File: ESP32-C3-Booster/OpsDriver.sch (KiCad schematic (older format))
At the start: 14 parts, among them U501 DRV8873HPWPR

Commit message: Completed first pass ESP32-C3-Booster.
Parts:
- added R505: 2.7K, Resistors_SMD:R_0603, symbol R
- added R506, R507: 10K, Resistors_SMD:R_0603, symbol R
- added U502: VO615A, Housings_SOIC:SO-4_7.6x3.6mm_Pitch2.54mm, symbol VO615A
- R501: value 220K -> 10K; Mouser Part Number 279-CRGCQ0603F220K -> 279-CRGCQ0603F10K
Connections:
- net +3V3: now also R506.1, R507.1
- net GND: now also U502.3
- net IN_A: now also R505.2; no longer U501.7 (EN/IN1)
- net IN_B: now also U502.1; no longer U501.8 (PH/IN2)
- new net: R507.2, U501.7 (EN/IN1)
- new net: R506.2, U501.8 (PH/IN2), U502.4
- new net: R505.1, U502.2
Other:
- moved on the sheet: TP501, TP502
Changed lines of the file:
@@
 LIBS:mcp9701at
 LIBS:MCP9700T-E_LT
+LIBS:ina180b
 LIBS:ESP32-C3-Booster-cache
 EELAYER 25 0
@@
 Comment4 ""
 $EndDescr
-Text HLabel 2500 2500 0    60   Input ~ 0
+Text HLabel 1050 2500 0    60   Input ~ 0
 IN_B
-Text HLabel 2500 2400 0    60   Input ~ 0
+Text HLabel 1050 2350 0    60   Input ~ 0
 IN_A
 Text HLabel 2500 2600 0    60   Input ~ 0
@@
 Sense_Neg
 $Comp
-L GND #PWR505
+L GND #PWR043
 U 1 1 630A7E57
 P 5250 1800
-F 0 "#PWR505" H 5250 1550 50  0001 C CNN
+F 0 "#PWR043" H 5250 1550 50  0001 C CNN
 F 1 "GND" H 5250 1650 50  0000 C CNN
 F 2 "" H 5250 1800 50  0001 C CNN
@@
 $EndComp
 $Comp
-L GND #PWR504
+L GND #PWR044
 U 1 1 630A7E58
 P 4250 3550
-F 0 "#PWR504" H 4250 3300 50  0001 C CNN
+F 0 "#PWR044" H 4250 3300 50  0001 C CNN
 F 1 "GND" H 4250 3400 50  0000 C CNN
 F 2 "" H 4250 3550 50  0001 C CNN
@@
 $EndComp
 $Comp
-L GND #PWR507
+L GND #PWR045
 U 1 1 630A7E5F
 P 6150 2750
-F 0 "#PWR507" H 6150 2500 50  0001 C CNN
+F 0 "#PWR045" H 6150 2500 50  0001 C CNN
 F 1 "GND" H 6150 2600 50  0000 C CNN
 F 2 "" H 6150 2750 50  0001 C CNN
@@
 $EndComp
 $Comp
-L GND #PWR506
+L GND #PWR046
 U 1 1 630A7E60
 P 5300 2550
-F 0 "#PWR506" H 5300 2300 50  0001 C CNN
+F 0 "#PWR046" H 5300 2300 50  0001 C CNN
 F 1 "GND" H 5300 2400 50  0000 C CNN
 F 2 "" H 5300 2550 50  0001 C CNN
@@
 $EndComp
 $Comp
-L GND #PWR502
+L GND #PWR047
 U 1 1 630A7E62
 P 3000 2250
-F 0 "#PWR502" H 3000 2000 50  0001 C CNN
+F 0 "#PWR047" H 3000 2000 50  0001 C CNN
 F 1 "GND" H 3000 2100 50  0000 C CNN
 F 2 "" H 3000 2250 50  0001 C CNN
@@
 $EndComp
 $Comp
-L +3.3V #PWR503
+L +3.3V #PWR048
 U 1 1 630A7E65
 P 3400 1100
-F 0 "#PWR503" H 3400 950 50  0001 C CNN
+F 0 "#PWR048" H 3400 950 50  0001 C CNN
 F 1 "+3.3V" H 3400 1240 50  0000 C CNN
 F 2 "" H 3400 1100 50  0001 C CNN
@@
 P 2600 2150
 F 0 "R501" V 2680 2150 50  0000 C CNN
-F 1 "220K" V 2600 2150 50  0000 C CNN
+F 1 "10K" V 2600 2150 50  0000 C CNN
 F 2 "Resistors_SMD:R_0603" V 2530 2150 50  0001 C CNN
 F 3 "" H 2600 2150 50  0001 C CNN
-F 4 "279-CRGCQ0603F220K " V 2600 2150 60  0001 C CNN "Mouser Part Number"
+F 4 "279-CRGCQ0603F10K " V 2600 2150 60  0001 C CNN "Mouser Part Number"
 	1    2600 2150
 	1    0    0    -1
 $EndComp
 $Comp
-L GND #PWR501
+L GND #PWR049
 U 1 1 630A7E67
 P 2600 2850
-F 0 "#PWR501" H 2600 2600 50  0001 C CNN
+F 0 "#PWR049" H 2600 2600 50  0001 C CNN
 F 1 "GND" H 2600 2700 50  0000 C CNN
 F 2 "" H 2600 2850 50  0001 C CNN
@@
 L TEST_1P TP502
 U 1 1 630A7E69
-P 3050 2750
-F 0 "TP502" H 3050 3020 50  0000 C CNN
-F 1 "IN_B" H 3050 2950 50  0000 C CNN
-F 2 "Measurement_Points:Measurement_Point_Round-SMD-Pad_Big" H 3250 2750 50  0001 C CNN
-F 3 "" H 3250 2750 50  0001 C CNN
-	1    3050 2750
+P 1300 2700
+F 0 "TP502" H 1300 2970 50  0000 C CNN
+F 1 "IN_B" H 1300 2900 50  0000 C CNN
+F 2 "Measurement_Points:Measurement_Point_Round-SMD-Pad_Big" H 1500 2700 50  0001 C CNN
+F 3 "" H 1500 2700 50  0001 C CNN
+	1    1300 2700
 	-1   0    0    1
 $EndComp
@@
 L TEST_1P TP501
 U 1 1 630A7E6A
-P 2850 2750
-F 0 "TP501" H 2850 3020 50  0000 C CNN
-F 1 "IN_A" H 2850 2950 50  0000 C CNN
-F 2 "Measurement_Points:Measurement_Point_Round-SMD-Pad_Big" H 3050 2750 50  0001 C CNN
-F 3 "" H 3050 2750 50  0001 C CNN
-	1    2850 2750
+P 1100 2700
+F 0 "TP501" H 1100 2970 50  0000 C CNN
+F 1 "IN_A" H 1100 2900 50  0000 C CNN
+F 2 "Measurement_Points:Measurement_Point_Round-SMD-Pad_Big" H 1300 2700 50  0001 C CNN
+F 3 "" H 1300 2700 50  0001 C CNN
+	1    1100 2700
 	-1   0    0    1
 $EndComp
 Wire Wire Line
-	2500 2400 3550 2400
-Wire Wire Line
-	2500 2500 3550 2500
+	2450 2400 3550 2400
+Wire Wire Line
+	2100 2500 3550 2500
 Wire Wire Line
 	2500 2600 3550 2600
@@
 	3400 1100 3400 1300
 Wire Wire Line
-	3500 1300 3500 1150
-Wire Wire Line
-	3500 1150 3400 1150
+	3500 1150 3500 1300
+Wire Wire Line
+	2450 1150 3500 1150
 Connection ~ 3400 1150
 Wire Wire Line
@@
 Connection ~ 3000 2200
 Connection ~ 3450 2200
-Wire Wire Line
-	2850 2750 2850 2400
-Connection ~ 2850 2400
-Wire Wire Line
-	3050 2750 3050 2500
-Connection ~ 3050 2500
 Wire Wire Line
 	3300 2750 3300 2600
@@
 	1    0    0    -1
 $EndComp
+Wire Wire Line
+	1050 2500 1500 2500
+Wire Wire Line
+	1300 2500 1300 2700
+Wire Wire Line
+	1050 2350 1150 2350
+Wire Wire Line
+	1100 2350 1100 2700
+$Comp
+L VO615A U502
+U 1 1 630BFB12
+P 1800 2400
+F 0 "U502" H 1700 2200 50  0000 L CNN
+F 1 "VO615A" H 1800 2600 50  0000 L CNN
+F 2 "Housings_SOIC:SO-4_7.6x3.6mm_Pitch2.54mm" H 1600 2200 50  0001 L CIN
+F 3 "" H 1800 2400 50  0001 L CNN
+F 4 "78-VO615A-7X017T" H 1800 2400 60  0001 C CNN "Mouser Part Number"
+	1    1800 2400
+	1    0    0    1
+$EndComp
+$Comp
+L R R507
+U 1 1 630BFBF6
+P 2450 2150
+F 0 "R507" V 2530 2150 50  0000 C CNN
+F 1 "10K" V 2450 2150 50  0000 C CNN
+F 2 "Resistors_SMD:R_0603" V 2380 2150 50  0001 C CNN
+F 3 "" H 2450 2150 50  0001 C CNN
+F 4 "279-CRGCQ0603F10K " V 2450 2150 60  0001 C CNN "Mouser Part Number"
+	1    2450 2150
+	1    0    0    -1
+$EndComp
+Wire Wire Line
+	2450 2300 2450 2400
+Wire Wire Line
+	2450 2000 2450 1150
+$Comp
+L R R506
+U 1 1 630BFE77
+P 2300 2150
+F 0 "R506" V 2380 2150 50  0000 C CNN
+F 1 "10K" V 2300 2150 50  0000 C CNN
+F 2 "Resistors_SMD:R_0603" V 2230 2150 50  0001 C CNN
+F 3 "" H 2300 2150 50  0001 C CNN
+F 4 "279-CRGCQ0603F10K " V 2300 2150 60  0001 C CNN "Mouser Part Number"
+	1    2300 2150
+	1    0    0    -1
+$EndComp
+Wire Wire Line
+	2300 2000 2450 2000
+$Comp
+L R R505
+U 1 1 630C0001
+P 1300 2300
+F 0 "R505" V 1380 2300 50  0000 C CNN
+F 1 "2.7K" V 1300 2300 50  0000 C CNN
+F 2 "Resistors_SMD:R_0603" V 1230 2300 50  0001 C CNN
+F 3 "" H 1300 2300 50  0001 C CNN
+F 4 "603-AC0603FR-132K7L" V 1300 2300 60  0001 C CNN "Mouser Part Number"
+	1    1300 2300
+	0    1    1    0
+$EndComp
+Wire Wire Line
+	1500 2300 1450 2300
+Connection ~ 1300 2500
+Wire Wire Line
+	1150 2350 1150 2300
+Connection ~ 1100 2350
+Wire Wire Line
+	2300 2300 2300 2500
+Connection ~ 2300 2500
+$Comp
+L GND #PWR050
+U 1 1 630C0BE3
+P 2100 2150
+F 0 "#PWR050" H 2100 1900 50  0001 C CNN
+F 1 "GND" H 2100 2000 50  0000 C CNN
+F 2 "" H 2100 2150 50  0001 C CNN
+F 3 "" H 2100 2150 50  0001 C CNN
+	1    2100 2150
+	-1   0    0    1
+$EndComp
+Wire Wire Line
+	2100 2150 2100 2300
 $EndSCHEMATC

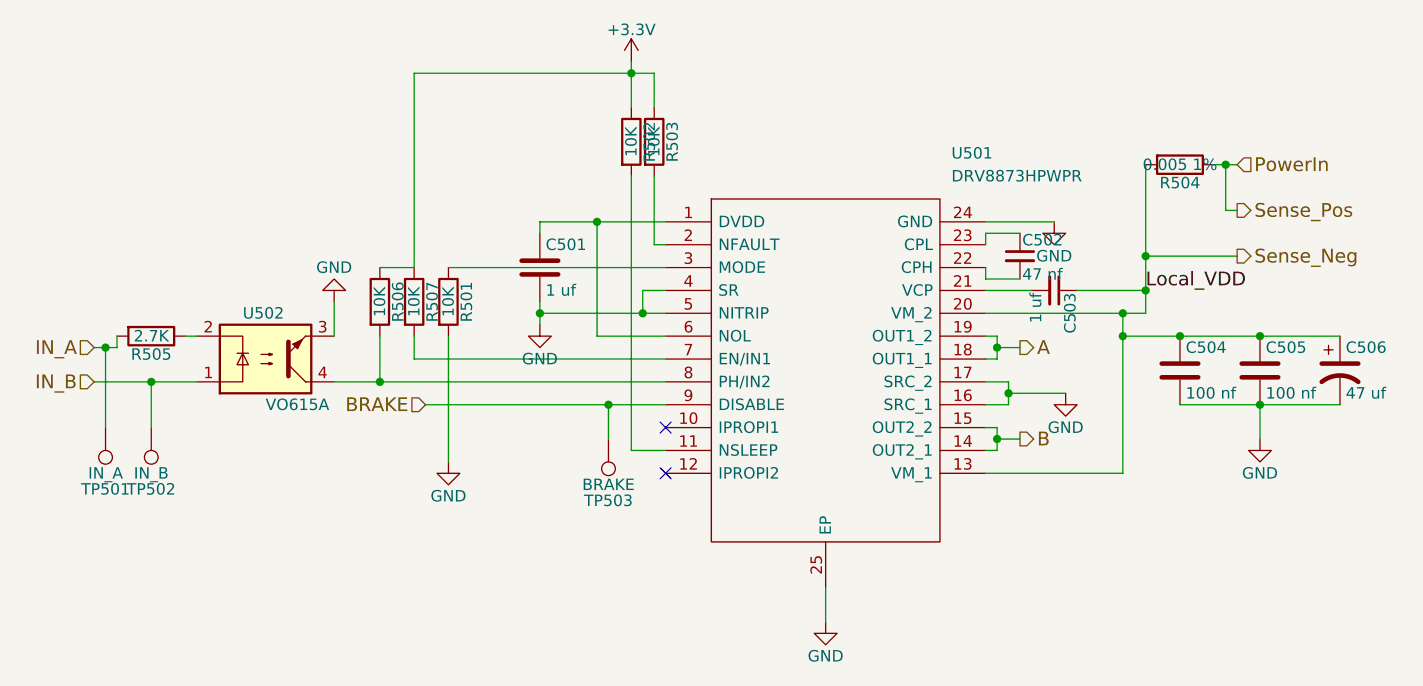
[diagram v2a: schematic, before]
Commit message: Updates to the Alt_H and Alt_L input handling in the Booster.
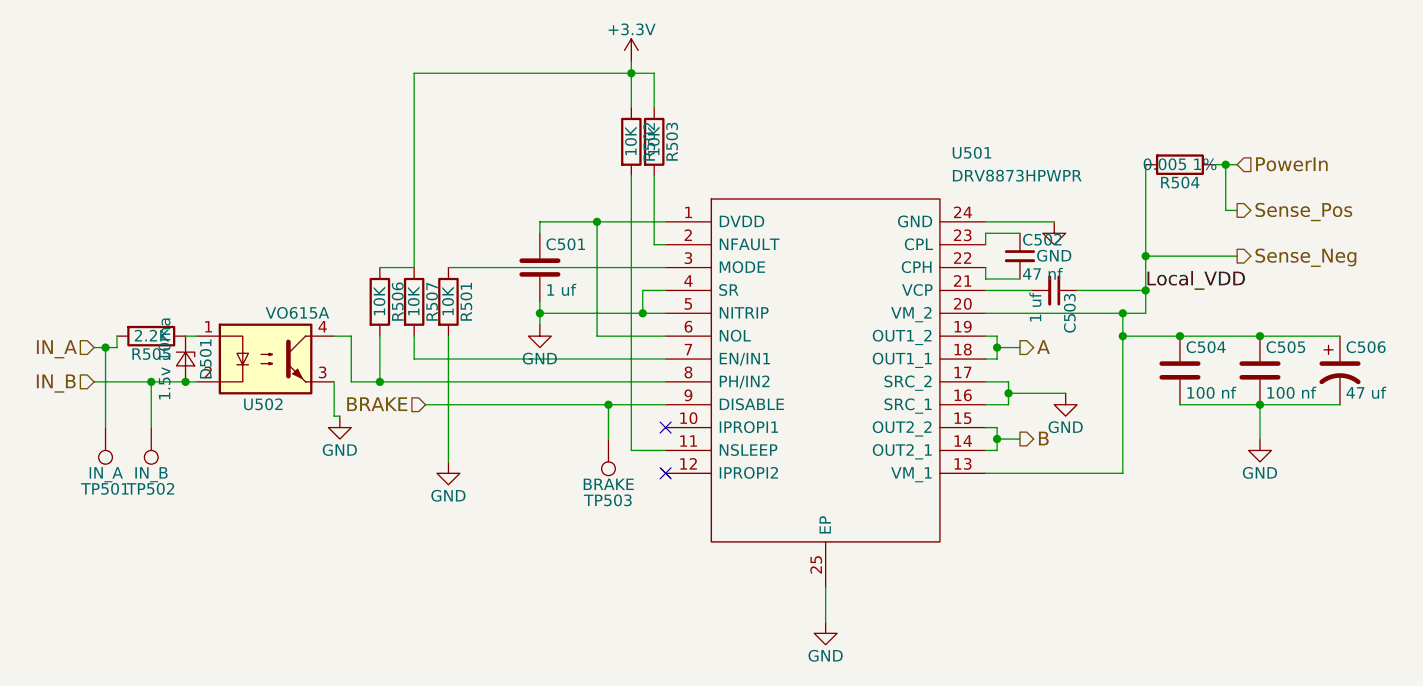
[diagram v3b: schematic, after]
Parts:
- added D501: 1.5v 10ma, Diodes_SMD:D_SOD-323, symbol D_Zener_Small
- R505: value 2.7K -> 2.2K; Mouser Part Number 603-AC0603FR-132K7L -> 603-AC0603FR-072K2L
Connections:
- net IN_B: now also U502.2, D501.2 (A); no longer U502.1
- net at R505.1: now also U502.1, D501.1 (K); no longer U502.2
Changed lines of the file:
@@
 	2450 2400 3550 2400
-Wire Wire Line
-	2100 2500 3550 2500
 Wire Wire Line
 	2500 2600 3550 2600
@@
 $EndComp
 Wire Wire Line
-	1050 2500 1500 2500
-Wire Wire Line
 	1300 2500 1300 2700
-Wire Wire Line
-	1050 2350 1150 2350
 Wire Wire Line
 	1100 2350 1100 2700
@@
 F 4 "78-VO615A-7X017T" H 1800 2400 60  0001 C CNN "Mouser Part Number"
 	1    1800 2400
-	1    0    0    1
+	1    0    0    -1
 $EndComp
 $Comp
@@
 P 1300 2300
 F 0 "R505" V 1380 2300 50  0000 C CNN
-F 1 "2.7K" V 1300 2300 50  0000 C CNN
+F 1 "2.2K" V 1300 2300 50  0000 C CNN
 F 2 "Resistors_SMD:R_0603" V 1230 2300 50  0001 C CNN
 F 3 "" H 1300 2300 50  0001 C CNN
-F 4 "603-AC0603FR-132K7L" V 1300 2300 60  0001 C CNN "Mouser Part Number"
+F 4 "603-AC0603FR-072K2L" V 1300 2300 60  0001 C CNN "Mouser Part Number"
 	1    1300 2300
 	0    1    1    0
 $EndComp
-Wire Wire Line
-	1500 2300 1450 2300
 Connection ~ 1300 2500
-Wire Wire Line
-	1150 2350 1150 2300
 Connection ~ 1100 2350
 Wire Wire Line
 	2300 2300 2300 2500
-Connection ~ 2300 2500
 $Comp
 L GND #PWR050
 U 1 1 630C0BE3
-P 2100 2150
-F 0 "#PWR050" H 2100 1900 50  0001 C CNN
-F 1 "GND" H 2100 2000 50  0000 C CNN
-F 2 "" H 2100 2150 50  0001 C CNN
-F 3 "" H 2100 2150 50  0001 C CNN
-	1    2100 2150
-	-1   0    0    1
-$EndComp
-Wire Wire Line
-	2100 2150 2100 2300
+P 2125 2650
+F 0 "#PWR050" H 2125 2400 50  0001 C CNN
+F 1 "GND" H 2125 2500 50  0000 C CNN
+F 2 "" H 2125 2650 50  0001 C CNN
+F 3 "" H 2125 2650 50  0001 C CNN
+	1    2125 2650
+	1    0    0    -1
+$EndComp
+Wire Wire Line
+	2100 2500 2100 2650
+Wire Wire Line
+	2100 2650 2125 2650
+Wire Wire Line
+	2100 2300 2175 2300
+Wire Wire Line
+	2175 2300 2175 2500
+Wire Wire Line
+	2175 2500 3550 2500
+Connection ~ 2300 2500
+Wire Wire Line
+	1500 2300 1450 2300
+Wire Wire Line
+	1050 2350 1150 2350
+Wire Wire Line
+	1150 2350 1150 2300
+Wire Wire Line
+	1050 2500 1500 2500
+$Comp
+L D_Zener_Small D501
+U 1 1 630E475C
+P 1450 2400
+F 0 "D501" H 1450 2490 50  0000 C CNN
+F 1 "1.5v 10ma" H 1450 2310 50  0000 C CNN
+F 2 "Diodes_SMD:D_SOD-323" V 1450 2400 50  0001 C CNN
+F 3 "" V 1450 2400 50  0001 C CNN
+F 4 "610-CMDZ1L8TR" H 1450 2400 60  0001 C CNN "Mouser Part Number"
+	1    1450 2400
+	0    1    1    0
+$EndComp
+Connection ~ 1450 2500
 $EndSCHEMATC
